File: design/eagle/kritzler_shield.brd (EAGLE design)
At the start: 66 x 53.5 mm, 20 parts, among them X1 1751264, X2 1751264

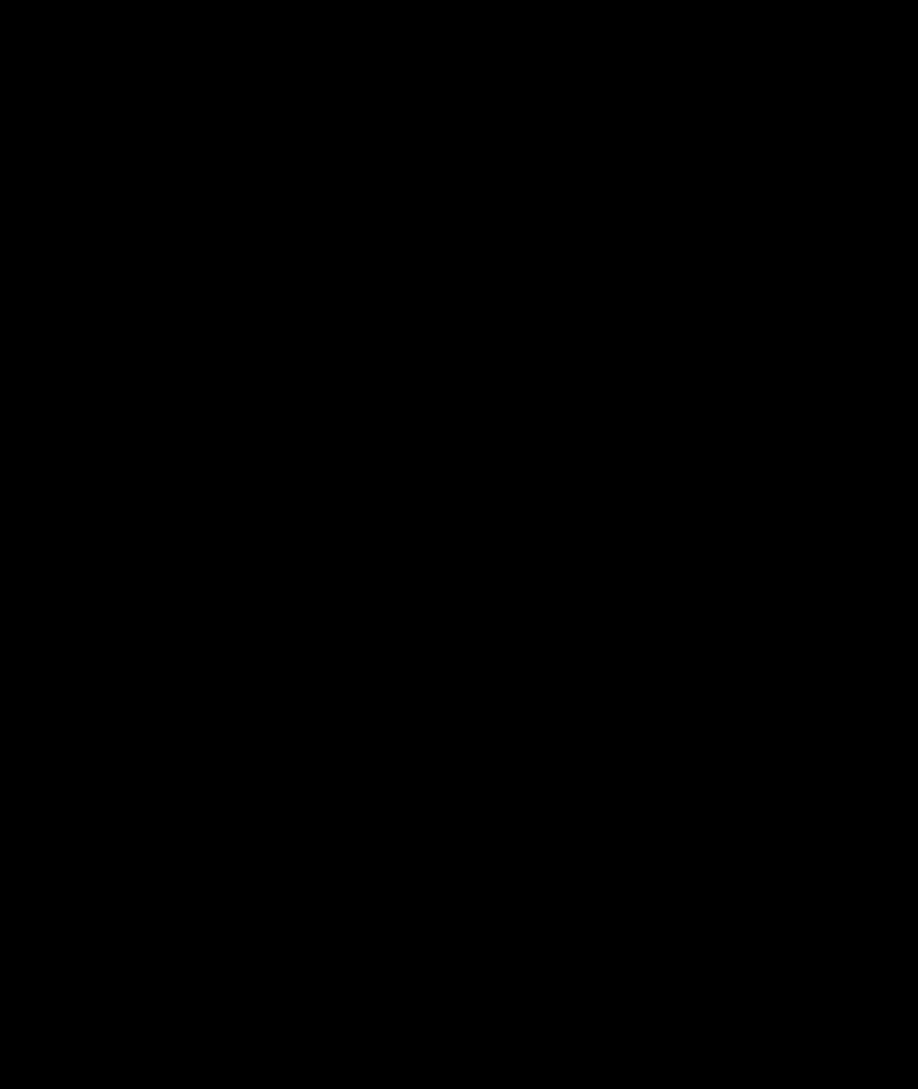
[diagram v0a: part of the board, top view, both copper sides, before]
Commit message: Added real-time pen location tracking and loads of Javadoc comments
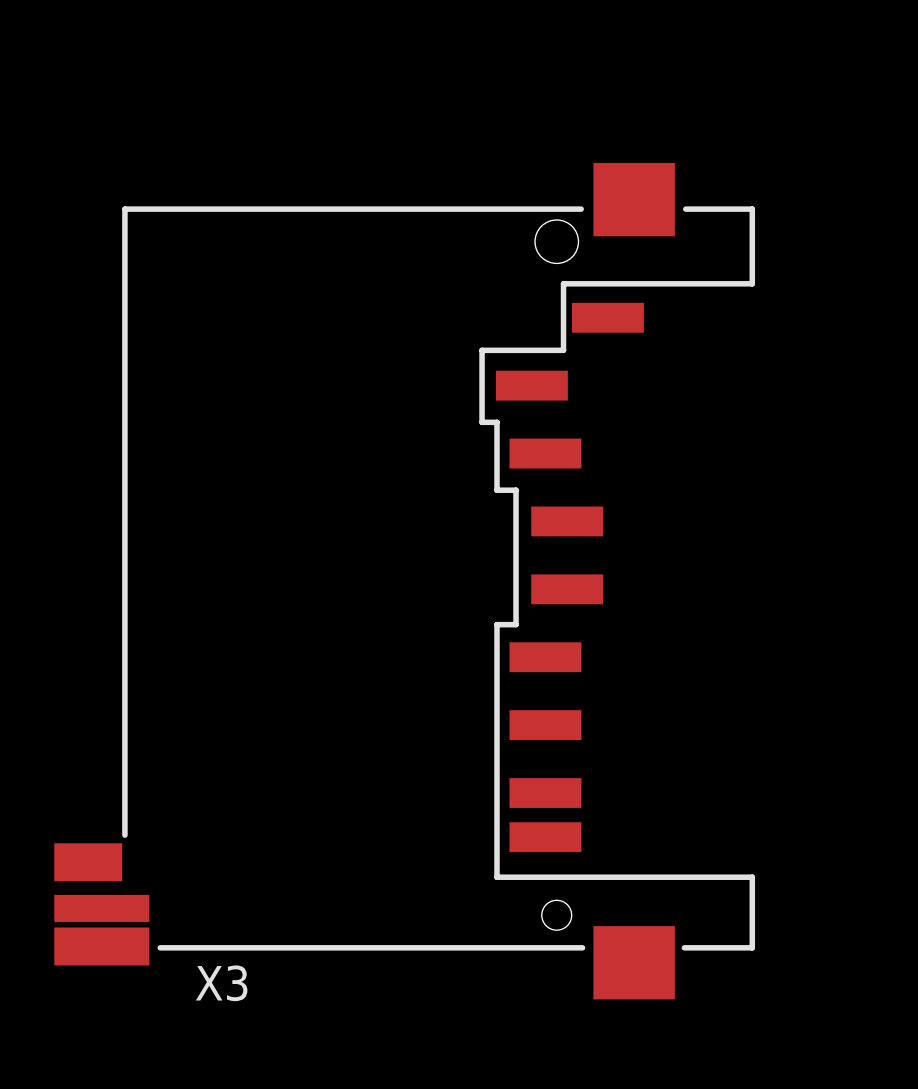
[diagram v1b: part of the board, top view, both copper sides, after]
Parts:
- added X3: FPS009-3002, con-yamaichi:FPS009-3000
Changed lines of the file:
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@@
 <?xml version="1.0" encoding="utf-8"?>
 <!DOCTYPE eagle SYSTEM "eagle.dtd">
-<eagle version="6.1">
+<eagle version="6.2">
 <drawing>
 <settings>
@@
 <layer number="215" name="215bmp" color="7" fill="1" visible="yes" active="yes"/>
 <layer number="216" name="216bmp" color="7" fill="1" visible="yes" active="yes"/>
+<layer number="217" name="217bmp" color="18" fill="1" visible="no" active="no"/>
+<layer number="218" name="218bmp" color="19" fill="1" visible="no" active="no"/>
+<layer number="219" name="219bmp" color="20" fill="1" visible="no" active="no"/>
+<layer number="220" name="220bmp" color="21" fill="1" visible="no" active="no"/>
+<layer number="221" name="221bmp" color="22" fill="1" visible="no" active="no"/>
+<layer number="222" name="222bmp" color="23" fill="1" visible="no" active="no"/>
+<layer number="223" name="223bmp" color="24" fill="1" visible="no" active="no"/>
+<layer number="224" name="224bmp" color="25" fill="1" visible="no" active="no"/>
 <layer number="250" name="Descript" color="3" fill="1" visible="no" active="no"/>
 <layer number="251" name="SMDround" color="12" fill="11" visible="no" active="no"/>
@@
 </element>
 <element name="U$8" library="ohw-logo" package="OSHW_FILLX150_NOTEXT" value="" x="6.6675" y="23.8125" rot="R90"/>
+<element name="X3" library="con-yamaichi" package="FPS009-3000" value="FPS009-3002" x="-26.67" y="29.21">
+<attribute name="OC_NEWARK" value="unknown" x="-26.67" y="29.21" size="1.778" layer="27" display="off"/>
+<attribute name="MPN" value="" x="-26.67" y="29.21" size="1.778" layer="27" display="off"/>
+<attribute name="MF" value="" x="-26.67" y="29.21" size="1.778" layer="27" display="off"/>
+<attribute name="OC_FARNELL" value="unknown" x="-26.67" y="29.21" size="1.778" layer="27" display="off"/>
+</element>
 </elements>
 <signals>
